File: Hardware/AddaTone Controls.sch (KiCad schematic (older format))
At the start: 18 parts, among them J1 Conn_01x20_Female, J2 Conn_01x20_Female, J3 PItch_In, J4 Harm1_In, J5 Harm2_In, J6 Freq_Scale_In, J7 DAC1_Out, J8 DAC2_Out, SW1 SW_Push, SW2 SW_Push, SW3 SW_SPST, SW4 SW_SPST

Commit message: Refinements to PCB
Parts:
- removed J1, J2: Conn_01x20_Female, Socket_Strips:Socket_Strip_Straight_1x20_Pitch2.54mm, symbol Connector:Conn_01x20_Female
- added J1: Conn_01x10_Male, Pin_Headers:Pin_Header_Straight_1x10_Pitch2.54mm, symbol Connector:Conn_01x10_Male
- added J2: Conn_01x12_Male, Pin_Headers:Pin_Header_Straight_1x12_Pitch2.54mm, symbol Connector:Conn_01x12_Male
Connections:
- net labels removed: ADC_CS, ADC_Clock, ADC_Data, DAC_BCLK, DAC_DATA, DAC_LRCLK, FPGA_DONE, FPGA_RESET, FPGA_SCK, FPGA_SI, FPGA_SO, FPGA_SS, MCO2_CLOCK_OUT
- wire segments 94 -> 54
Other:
- moved on the sheet: CTune1, FTune1, FreqScale1, Harm1, Harm2, HarmCount1, J3, J4, J5, J6, J7, J8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

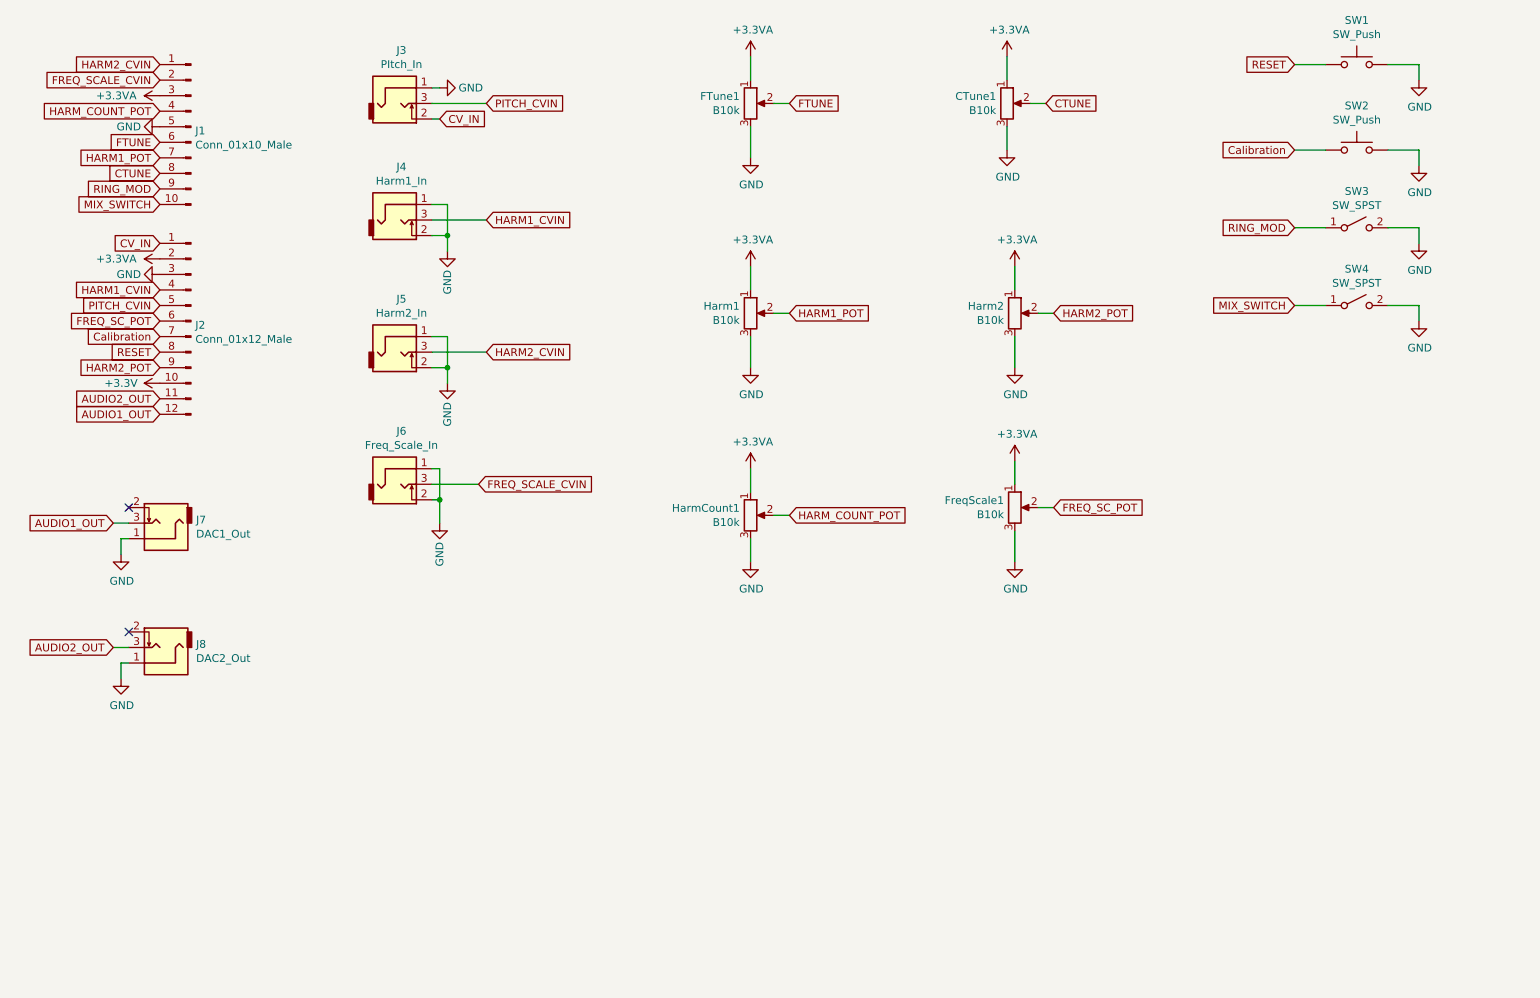
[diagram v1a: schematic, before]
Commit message: Updated FPGA programming code to use correct pin for Reset; Minor PCB corrections
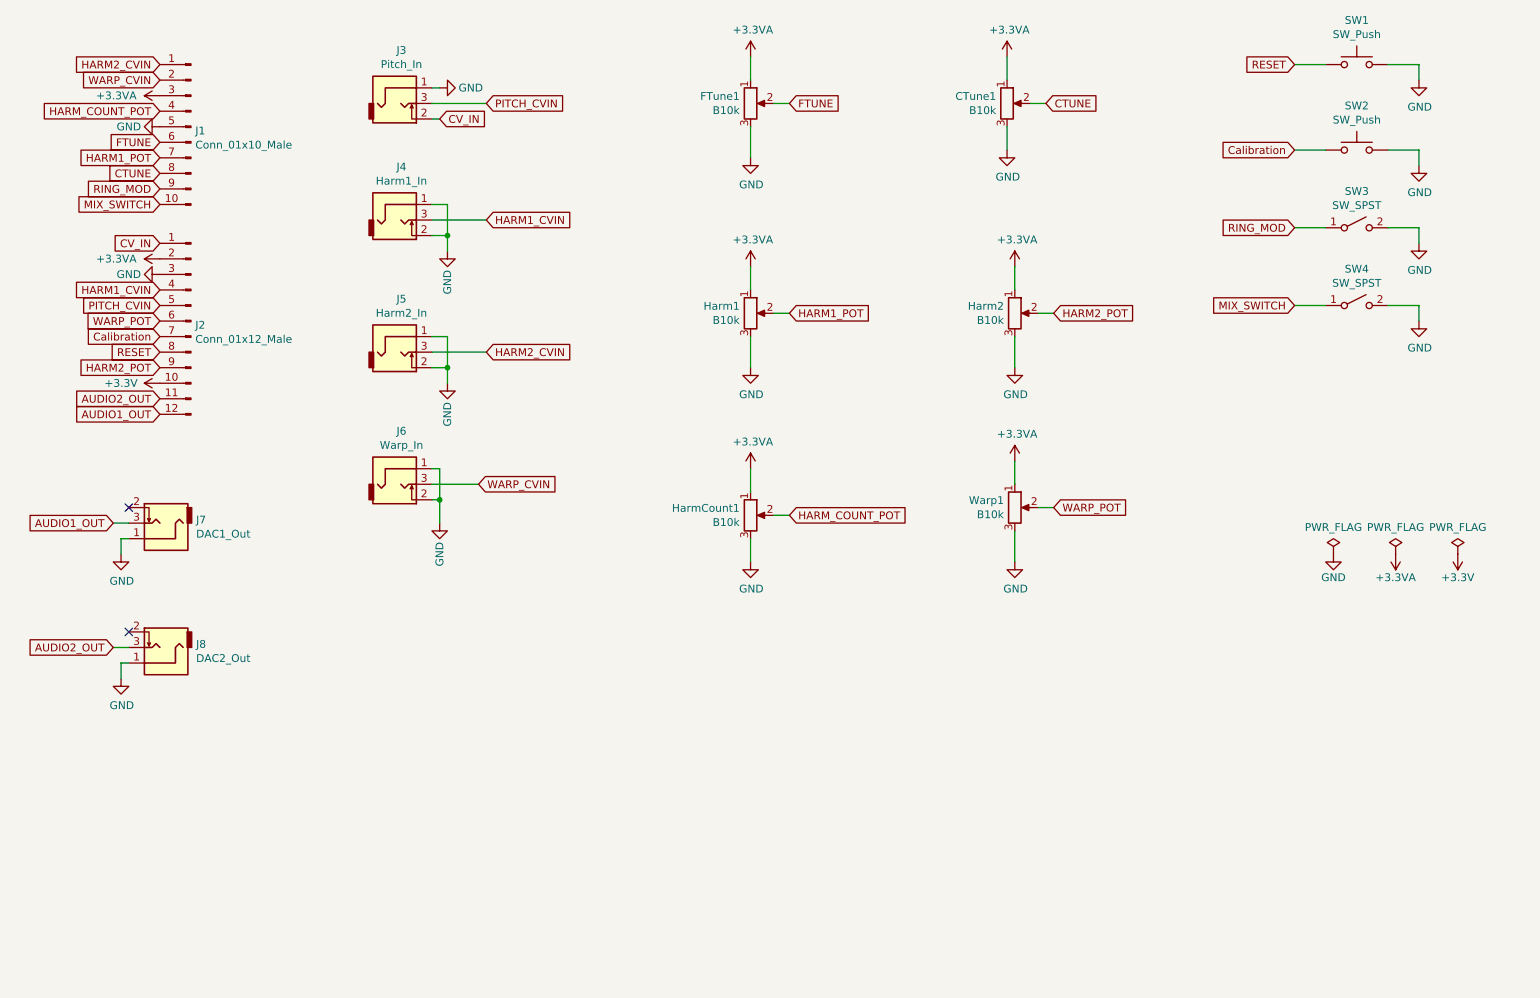
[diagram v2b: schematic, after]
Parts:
- J3: value PItch_In -> Pitch_In
- J6: value Freq_Scale_In -> Warp_In
- renumbered FreqScale1 to Warp1
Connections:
- net FREQ_SCALE_CVIN renamed WARP_CVIN
- net FREQ_SC_POT renamed WARP_POT
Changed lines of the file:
@@
 MIX_SWITCH
 $Comp
-L Device:R_POT FreqScale1
+L Device:R_POT Warp1
 U 1 1 5C7E8920
 P 7350 3900
-F 0 "FreqScale1" H 7280 3946 50  0000 R CNN
+F 0 "Warp1" H 7280 3946 50  0000 R CNN
 F 1 "B10k" H 7280 3855 50  0000 R CNN
 F 2 "Custom_Footprints:Alpha_9mm_Potentiometer" H 7350 3900 50  0001 C CNN
@@
 $EndComp
 Text GLabel 7600 3900 2    50   Input ~ 0
-FREQ_SC_POT
+WARP_POT
 $Comp
 L power:+3.3VA #PWR022
@@
 P 3400 1300
 F 0 "J3" H 3404 1642 50  0000 C CNN
-F 1 "PItch_In" H 3404 1551 50  0000 C CNN
+F 1 "Pitch_In" H 3404 1551 50  0000 C CNN
 F 2 "Custom_Footprints:THONKICONN_hole" H 3400 1300 50  0001 C CNN
 F 3 "~" H 3400 1300 50  0001 C CNN
@@
 P 3400 3750
 F 0 "J6" H 3404 4092 50  0000 C CNN
-F 1 "Freq_Scale_In" H 3404 4001 50  0000 C CNN
+F 1 "Warp_In" H 3404 4001 50  0000 C CNN
 F 2 "Custom_Footprints:THONKICONN_hole" H 3400 3750 50  0001 C CNN
 F 3 "~" H 3400 3750 50  0001 C CNN
@@
 CV_IN
 Text GLabel 1850 2700 0    50   Input ~ 0
-FREQ_SC_POT
+WARP_POT
 Text GLabel 1850 1750 0    50   Input ~ 0
 CTUNE
@@
 RING_MOD
 Text GLabel 1850 1150 0    50   Input ~ 0
-FREQ_SCALE_CVIN
+WARP_CVIN
 Text GLabel 1850 2800 0    50   Input ~ 0
 Calibration
@@
 HARM2_CVIN
 Text GLabel 3900 3750 2    50   Input ~ 0
-FREQ_SCALE_CVIN
+WARP_CVIN
 $Comp
 L Switch:SW_Push SW1
@@
 	-1   0    0    -1
 $EndComp
+$Comp
+L power:PWR_FLAG #FLG0101
+U 1 1 5EA15FA7
+P 9400 4200
+F 0 "#FLG0101" H 9400 4275 50  0001 C CNN
+F 1 "PWR_FLAG" H 9400 4373 50  0000 C CNN
+F 2 "" H 9400 4200 50  0001 C CNN
+F 3 "~" H 9400 4200 50  0001 C CNN
+	1    9400 4200
+	1    0    0    -1
+$EndComp
+$Comp
+L power:GND #PWR0101
+U 1 1 5EA1643A
+P 9400 4200
+F 0 "#PWR0101" H 9400 3950 50  0001 C CNN
+F 1 "GND" H 9400 4050 50  0000 C CNN
+F 2 "" H 9400 4200 50  0001 C CNN
+F 3 "" H 9400 4200 50  0001 C CNN
+	1    9400 4200
+	1    0    0    -1
+$EndComp
+$Comp
+L power:+3.3VA #PWR0102
+U 1 1 5EA169A5
+P 9800 4200
+F 0 "#PWR0102" H 9800 4050 50  0001 C CNN
+F 1 "+3.3VA" H 9800 4350 50  0000 C CNN
+F 2 "" H 9800 4200 50  0001 C CNN
+F 3 "" H 9800 4200 50  0001 C CNN
+	1    9800 4200
+	-1   0    0    1
+$EndComp
+$Comp
+L power:PWR_FLAG #FLG0102
+U 1 1 5EA171ED
+P 9800 4200
+F 0 "#FLG0102" H 9800 4275 50  0001 C CNN
+F 1 "PWR_FLAG" H 9800 4373 50  0000 C CNN
+F 2 "" H 9800 4200 50  0001 C CNN
+F 3 "~" H 9800 4200 50  0001 C CNN
+	1    9800 4200
+	1    0    0    -1
+$EndComp
+$Comp
+L power:+3.3V #PWR0103
+U 1 1 5EA175C7
+P 10200 4200
+F 0 "#PWR0103" H 10200 4050 50  0001 C CNN
+F 1 "+3.3V" H 10200 4350 50  0000 C CNN
+F 2 "" H 10200 4200 50  0001 C CNN
+F 3 "" H 10200 4200 50  0001 C CNN
+	1    10200 4200
+	-1   0    0    1
+$EndComp
+$Comp
+L power:PWR_FLAG #FLG0103
+U 1 1 5EA180F0
+P 10200 4200
+F 0 "#FLG0103" H 10200 4275 50  0001 C CNN
+F 1 "PWR_FLAG" H 10200 4373 50  0000 C CNN
+F 2 "" H 10200 4200 50  0001 C CNN
+F 3 "~" H 10200 4200 50  0001 C CNN
+	1    10200 4200
+	1    0    0    -1
+$EndComp
 $EndSCHEMATC
